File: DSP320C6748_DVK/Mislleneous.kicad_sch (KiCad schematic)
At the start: 45 parts, among them IC17 MUN5211DW1T1G, IC18 MUN5211DW1T1G, SW1 SW_DIP_x08

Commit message: Schematic Corrections-II Done
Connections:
- net +3V3D: now also R229.2, R230.2, R231.2, R232.2; no longer R261.1, R262.1
- net GND: no longer R229.2, R230.2, R231.2, R232.2
- new net +5V: R261.1, R262.1
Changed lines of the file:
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@@
 	)
 	(symbol
-		(lib_id "power:+3V3")
-		(at 257.81 121.92 90)
-		(unit 1)
-		(body_style 1)
-		(exclude_from_sim no)
-		(in_bom yes)
-		(on_board yes)
-		(in_pos_files yes)
-		(dnp no)
-		(fields_autoplaced yes)
-		(property "Reference" "#PWR0376"
-			(at 261.62 121.92 0)
-			(hide yes)
-			(show_name no)
-			(do_not_autoplace no)
-			(effects
-				(font
-					(size 1.27 1.27)
-				)
-			)
-		)
-		(property "Value" "+3V3D"
-			(at 252.73 121.92 0)
-			(show_name no)
-			(do_not_autoplace no)
-			(effects
-				(font
-					(size 1.27 1.27)
-				)
-			)
-		)
-		(property "Footprint" ""
-			(at 257.81 121.92 0)
-			(hide yes)
-			(show_name no)
-			(do_not_autoplace no)
-			(effects
-				(font
-					(size 1.27 1.27)
-				)
-			)
-		)
-		(property "Datasheet" ""
-			(at 257.81 121.92 0)
-			(hide yes)
-			(show_name no)
-			(do_not_autoplace no)
-			(effects
-				(font
-					(size 1.27 1.27)
-				)
-			)
-		)
-		(property "Description" "Power symbol creates a global label with name \"+3V3\""
-			(at 257.81 121.92 0)
-			(hide yes)
-			(show_name no)
-			(do_not_autoplace no)
-			(effects
-				(font
-					(size 1.27 1.27)
-				)
-			)
-		)
-		(pin "1"
-		)
-		(instances
-			(project "DSP320C6748_DVK"
-				(path "/3a70ffc0-9fe7-4a5b-b3c2-23140355df82/1866fe1a-a792-425d-9c22-4cbe8219f03e"
-					(reference "#PWR0376")
-					(unit 1)
-				)
-			)
-		)
-	)
-	(symbol
 		(lib_id "LOGSUN:LGS-KC-10-XX")
 		(at 195.58 146.05 270)
@@
 	)
 	(symbol
+		(lib_id "power:+5V")
+		(at 257.81 153.67 90)
+		(unit 1)
+		(body_style 1)
+		(exclude_from_sim no)
+		(in_bom yes)
+		(on_board yes)
+		(in_pos_files yes)
+		(dnp no)
+		(fields_autoplaced yes)
+		(property "Reference" "#PWR0389"
+			(at 261.62 153.67 0)
+			(hide yes)
+			(show_name no)
+			(do_not_autoplace no)
+			(effects
+				(font
+					(size 1.27 1.27)
+				)
+			)
+		)
+		(property "Value" "+5V"
+			(at 254 153.6699 90)
+			(show_name no)
+			(do_not_autoplace no)
+			(effects
+				(font
+					(size 1.27 1.27)
+				)
+				(justify left)
+			)
+		)
+		(property "Footprint" ""
+			(at 257.81 153.67 0)
+			(hide yes)
+			(show_name no)
+			(do_not_autoplace no)
+			(effects
+				(font
+					(size 1.27 1.27)
+				)
+			)
+		)
+		(property "Datasheet" ""
+			(at 257.81 153.67 0)
+			(hide yes)
+			(show_name no)
+			(do_not_autoplace no)
+			(effects
+				(font
+					(size 1.27 1.27)
+				)
+			)
+		)
+		(property "Description" "Power symbol creates a global label with name \"+5V\""
+			(at 257.81 153.67 0)
+			(hide yes)
+			(show_name no)
+			(do_not_autoplace no)
+			(effects
+				(font
+					(size 1.27 1.27)
+				)
+			)
+		)
+		(pin "1"
+		)
+		(instances
+			(project "DSP320C6748_DVK"
+				(path "/3a70ffc0-9fe7-4a5b-b3c2-23140355df82/1866fe1a-a792-425d-9c22-4cbe8219f03e"
+					(reference "#PWR0389")
+					(unit 1)
+				)
+			)
+		)
+	)
+	(symbol
 		(lib_id "Device:R_Small")
 		(at 243.84 119.38 0)
@@
 	)
 	(symbol
-		(lib_id "power:+3V3")
-		(at 257.81 153.67 90)
+		(lib_id "Device:R_Small")
+		(at 261.62 121.92 90)
 		(unit 1)
 		(body_style 1)
@@
 		(in_pos_files yes)
 		(dnp no)
-		(fields_autoplaced yes)
-		(property "Reference" "#PWR0377"
-			(at 261.62 153.67 0)
-			(hide yes)
+		(property "Reference" "R261"
+			(at 263.398 123.444 90)
 			(show_name no)
 			(do_not_autoplace no)
 			(effects
 				(font
-					(size 1.27 1.27)
+					(size 1.016 1.016)
 				)
+				(justify left)
 			)
 		)
-		(property "Value" "+3V3D"
-			(at 252.73 153.67 0)
+		(property "Value" "330R,5%,1/16W"
+			(at 268.732 118.11 90)
 			(show_name no)
 			(do_not_autoplace no)
@@
 					(size 1.27 1.27)
 				)
+				(justify left)
 			)
 		)
 		(property "Footprint" ""
-			(at 257.81 153.67 0)
+			(at 261.62 121.92 0)
 			(hide yes)
 			(show_name no)
@@
 		)
 		(property "Datasheet" ""
-			(at 257.81 153.67 0)
+			(at 261.62 121.92 0)
 			(hide yes)
 			(show_name no)
@@
 			)
 		)
-		(property "Description" "Power symbol creates a global label with name \"+3V3\""
-			(at 257.81 153.67 0)
+		(property "Description" "Resistor, small symbol"
+			(at 261.62 121.92 0)
 			(hide yes)
 			(show_name no)
@@
 			)
 		)
+		(pin "2"
+		)
 		(pin "1"
 		)
@@
 			(project "DSP320C6748_DVK"
 				(path "/3a70ffc0-9fe7-4a5b-b3c2-23140355df82/1866fe1a-a792-425d-9c22-4cbe8219f03e"
-					(reference "#PWR0377")
+					(reference "R261")
 					(unit 1)
 				)
@@
 	)
 	(symbol
-		(lib_id "power:GND")
-		(at 48.26 143.51 90)
+		(lib_id "power:+5V")
+		(at 257.81 121.92 90)
 		(unit 1)
 		(body_style 1)
@@
 		(in_pos_files yes)
 		(dnp no)
-		(property "Reference" "#PWR0364"
-			(at 54.61 143.51 0)
-			(hide yes)
-			(show_name no)
-			(do_not_autoplace no)
-			(effects
-				(font
-					(size 1.27 1.27)
-				)
-			)
-		)
-		(property "Value" "GND"
-			(at 51.816 143.51 0)
-			(show_name no)
-			(do_not_autoplace no)
-			(effects
-				(font
-					(size 1.27 1.27)
-				)
-			)
-		)
-		(property "Footprint" ""
-			(at 48.26 143.51 0)
+		(fields_autoplaced yes)
+		(property "Reference" "#PWR0356"
+			(at 261.62 121.92 0)
 			(hide yes)
 			(show_name no)
@@
 			)
 		)
-		(property "Datasheet" ""
-			(at 48.26 143.51 0)
-			(hide yes)
-			(show_name no)
-			(do_not_autoplace no)
-			(effects
-				(font
-					(size 1.27 1.27)
-				)
-			)
-		)
-		(property "Description" "Power symbol creates a global label with name \"GND\" , ground"
-			(at 48.26 143.51 0)
-			(hide yes)
-			(show_name no)
-			(do_not_autoplace no)
-			(effects
-				(font
-					(size 1.27 1.27)
-				)
-			)
-		)
-		(pin "1"
-		)
-		(instances
-			(project "DSP320C6748_DVK"
-				(path "/3a70ffc0-9fe7-4a5b-b3c2-23140355df82/1866fe1a-a792-425d-9c22-4cbe8219f03e"
-					(reference "#PWR0364")
-					(unit 1)
-				)
-			)
-		)
-	)
-	(symbol
-		(lib_id "Device:R_Small")
-		(at 261.62 121.92 90)
-		(unit 1)
-		(body_style 1)
-		(exclude_from_sim no)
-		(in_bom yes)
-		(on_board yes)
-		(in_pos_files yes)
-		(dnp no)
-		(property "Reference" "R261"
-			(at 263.398 123.444 90)
-			(show_name no)
-			(do_not_autoplace no)
-			(effects
-				(font
-					(size 1.016 1.016)
-				)
-				(justify left)
-			)
-		)
-		(property "Value" "330R,5%,1/16W"
-			(at 268.732 118.11 90)
+		(property "Value" "+5V"
+			(at 254 121.9199 90)
 			(show_name no)
 			(do_not_autoplace no)
@@
 		)
 		(property "Footprint" ""
-			(at 261.62 121.92 0)
+			(at 257.81 121.92 0)
 			(hide yes)
 			(show_name no)
@@
 		)
 		(property "Datasheet" ""
-			(at 261.62 121.92 0)
+			(at 257.81 121.92 0)
 			(hide yes)
 			(show_name no)
@@
 			)
 		)
-		(property "Description" "Resistor, small symbol"
-			(at 261.62 121.92 0)
+		(property "Description" "Power symbol creates a global label with name \"+5V\""
+			(at 257.81 121.92 0)
 			(hide yes)
 			(show_name no)
@@
 			)
 		)
-		(pin "2"
-		)
 		(pin "1"
 		)
@@
 			(project "DSP320C6748_DVK"
 				(path "/3a70ffc0-9fe7-4a5b-b3c2-23140355df82/1866fe1a-a792-425d-9c22-4cbe8219f03e"
-					(reference "R261")
+					(reference "#PWR0356")
 					(unit 1)
 				)
@@
 					(unit 1)
 				)
+			)
+		)
+	)
+	(symbol
+		(lib_id "power:+3V3")
+		(at 48.26 143.51 0)
+		(unit 1)
+		(body_style 1)
+		(exclude_from_sim no)
+		(in_bom yes)
+		(on_board yes)
+		(in_pos_files yes)
+		(dnp no)
+		(fields_autoplaced yes)
+		(property "Reference" "#PWR0384"
+			(at 48.26 147.32 0)
+			(hide yes)
+			(show_name no)
+			(do_not_autoplace no)
+			(effects
+				(font
+					(size 1.27 1.27)
+				)
+			)
+		)
+		(property "Value" "+3V3D"
+			(at 48.26 138.43 0)
+			(show_name no)
+			(do_not_autoplace no)
+			(effects
+				(font
+					(size 1.27 1.27)
+				)
+			)
+		)
+		(property "Footprint" ""
+			(at 48.26 143.51 0)
+			(hide yes)
+			(show_name no)
+			(do_not_autoplace no)
+			(effects
+				(font
+					(size 1.27 1.27)
+				)
+			)
+		)
+		(property "Datasheet" ""
+			(at 48.26 143.51 0)
+			(hide yes)
+			(show_name no)
+			(do_not_autoplace no)
+			(effects
+				(font
+					(size 1.27 1.27)
+				)
+			)
+		)
+		(property "Description" "Power symbol creates a global label with name \"+3V3\""
+			(at 48.26 143.51 0)
+			(hide yes)
+			(show_name no)
+			(do_not_autoplace no)
+			(effects
+				(font
+					(size 1.27 1.27)
+				)
+			)
+		)
+		(pin "1"
+		)
+		(instances
+			(project "DSP320C6748_DVK"
+				(path "/3a70ffc0-9fe7-4a5b-b3c2-23140355df82/1866fe1a-a792-425d-9c22-4cbe8219f03e"
+					(reference "#PWR0384")
+					(unit 1)
+				)

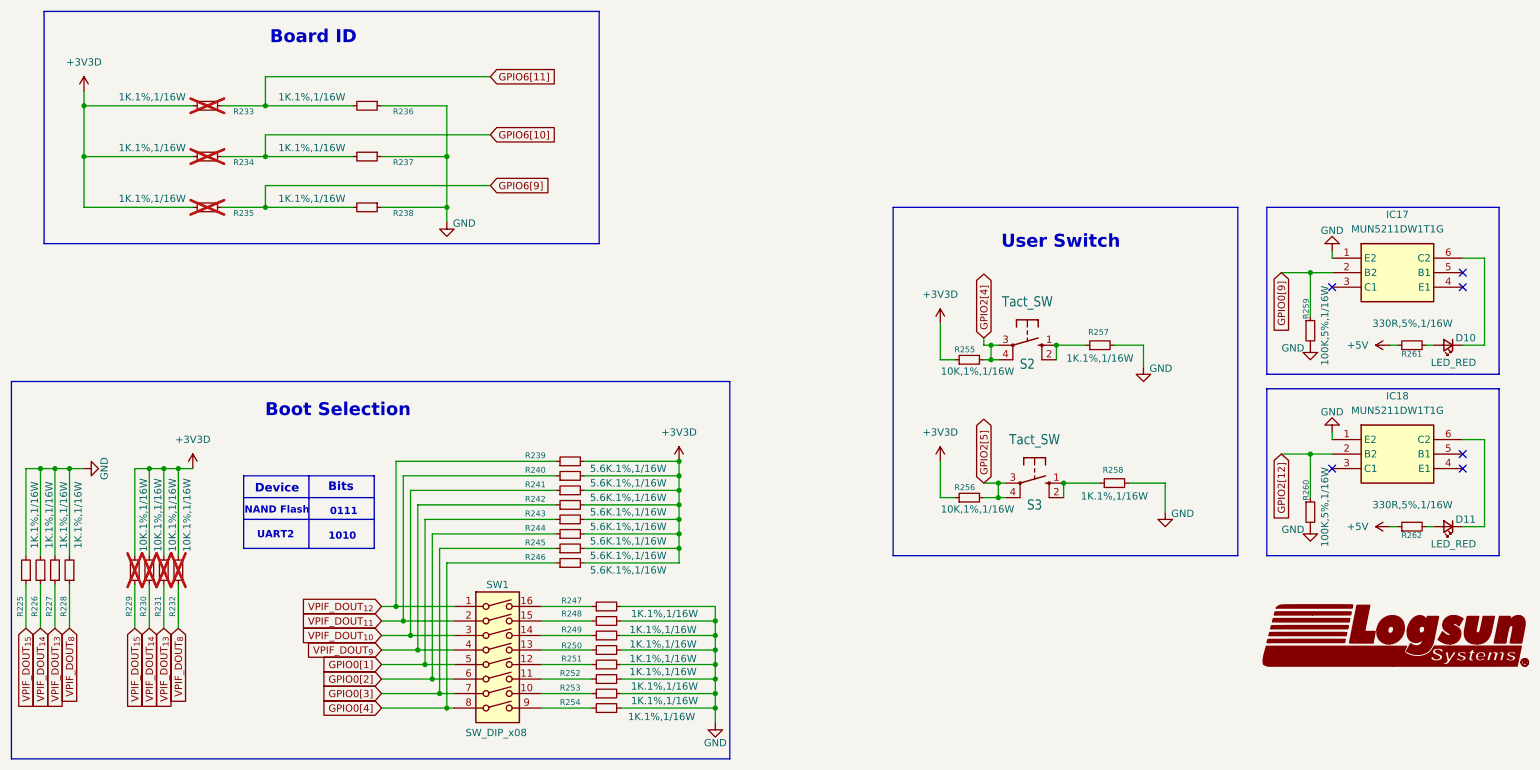
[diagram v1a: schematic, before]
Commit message: DC jack Replaced With Type-C, ADC and RTC section added
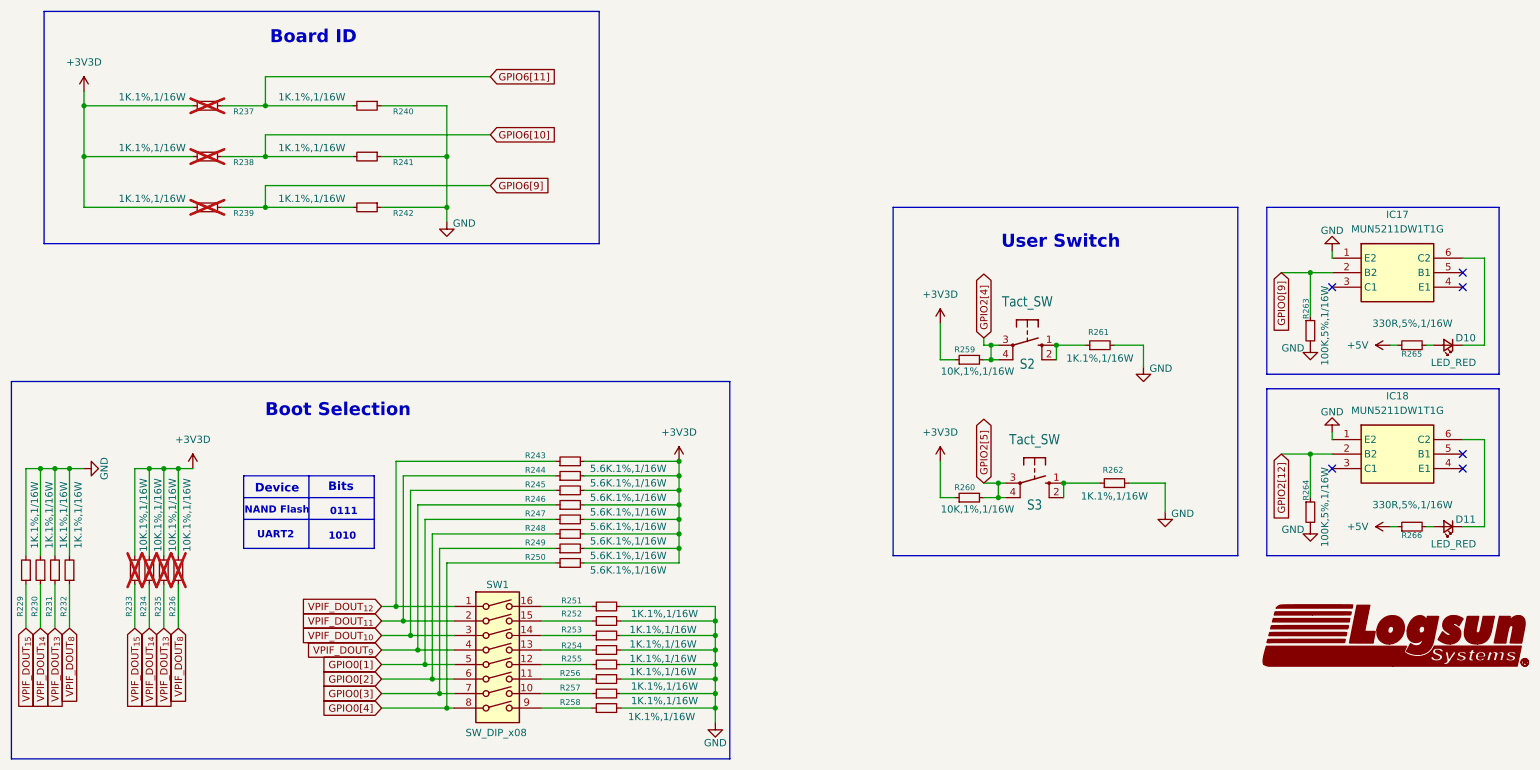
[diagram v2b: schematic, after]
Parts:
- renumbered R225 to R229, R226 to R230, R227 to R231, R228 to R232, R229 to R233, R230 to R234, R231 to R235, R232 to R236, R233 to R237, R234 to R238, R235 to R239, R236 to R240, R237 to R241, R238 to R242, R239 to R243, R240 to R244, R241 to R245, R242 to R246, R243 to R247, R244 to R248, R245 to R249, R246 to R250, R247 to R251, R248 to R252, R249 to R253, R250 to R254, R251 to R255, R252 to R256, R253 to R257, R254 to R258, R255 to R259, R256 to R260, R257 to R261, R258 to R262, R259 to R263, R260 to R264, R261 to R265, R262 to R266

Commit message: Scheamtic Re-annotation done, Some footprints assigned
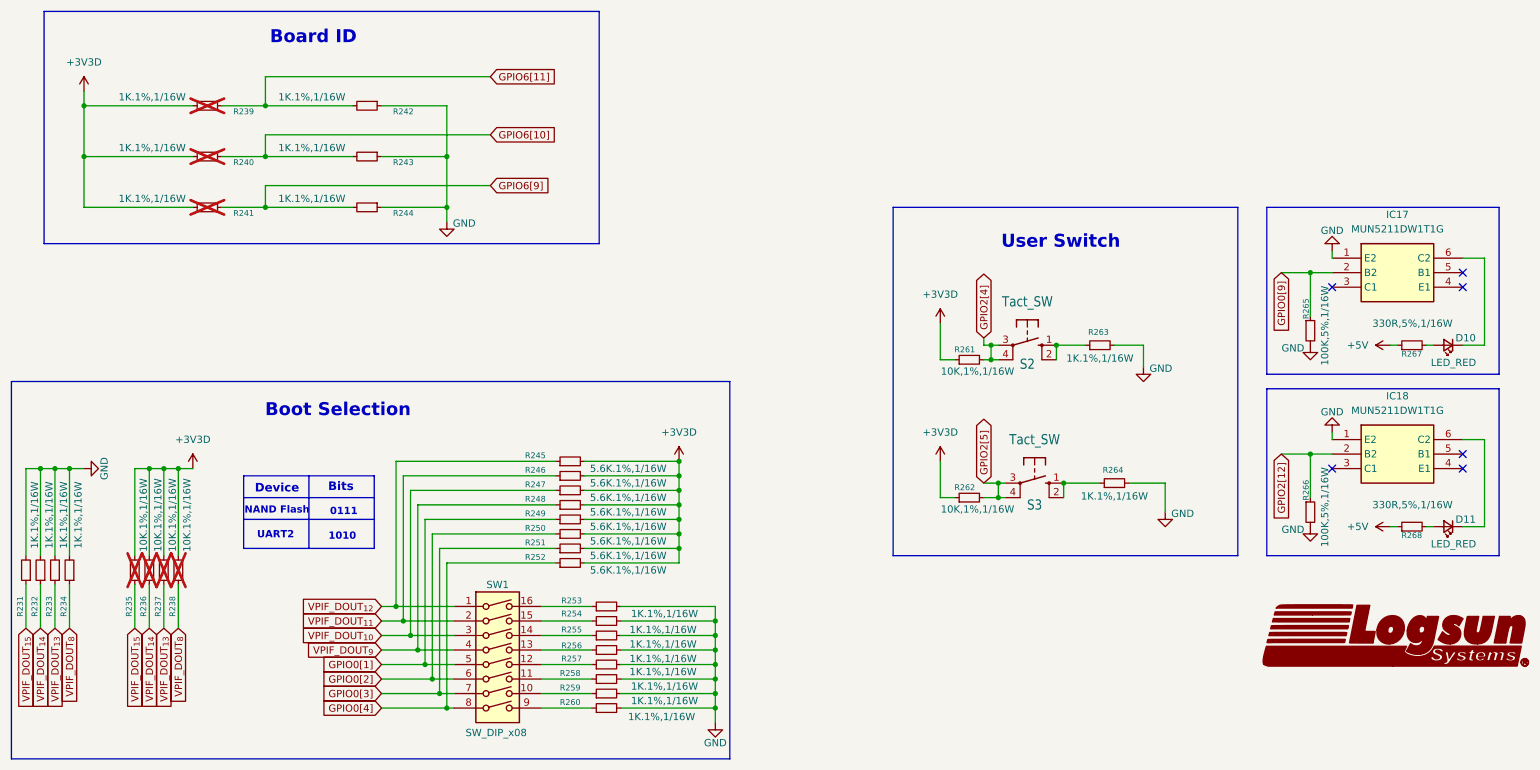
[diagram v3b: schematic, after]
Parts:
- R231: renamed from R229; footprint (none) -> Resistor_SMD:R_0603_1608Metric_Pad0.98x0.95mm_HandSolder
- R232: renamed from R230; footprint (none) -> Resistor_SMD:R_0603_1608Metric_Pad0.98x0.95mm_HandSolder
- R233: renamed from R231; footprint (none) -> Resistor_SMD:R_0603_1608Metric_Pad0.98x0.95mm_HandSolder
- R234: renamed from R232; footprint (none) -> Resistor_SMD:R_0603_1608Metric_Pad0.98x0.95mm_HandSolder
- R235: renamed from R233; footprint (none) -> Resistor_SMD:R_0603_1608Metric_Pad0.98x0.95mm_HandSolder
- R236: renamed from R234; footprint (none) -> Resistor_SMD:R_0603_1608Metric_Pad0.98x0.95mm_HandSolder
- R237: renamed from R235; footprint (none) -> Resistor_SMD:R_0603_1608Metric_Pad0.98x0.95mm_HandSolder
- R238: renamed from R236; footprint (none) -> Resistor_SMD:R_0603_1608Metric_Pad0.98x0.95mm_HandSolder
- R239: renamed from R237; footprint (none) -> Resistor_SMD:R_0603_1608Metric_Pad0.98x0.95mm_HandSolder
- R240: renamed from R238; footprint (none) -> Resistor_SMD:R_0603_1608Metric_Pad0.98x0.95mm_HandSolder
- R241: renamed from R239; footprint (none) -> Resistor_SMD:R_0603_1608Metric_Pad0.98x0.95mm_HandSolder
- R242: renamed from R240; footprint (none) -> Resistor_SMD:R_0603_1608Metric_Pad0.98x0.95mm_HandSolder
- R243: renamed from R241; footprint (none) -> Resistor_SMD:R_0603_1608Metric_Pad0.98x0.95mm_HandSolder
- R244: renamed from R242; footprint (none) -> Resistor_SMD:R_0603_1608Metric_Pad0.98x0.95mm_HandSolder
- R245: renamed from R243; footprint (none) -> Resistor_SMD:R_0603_1608Metric_Pad0.98x0.95mm_HandSolder
- R246: renamed from R244; footprint (none) -> Resistor_SMD:R_0603_1608Metric_Pad0.98x0.95mm_HandSolder
- R247: renamed from R245; footprint (none) -> Resistor_SMD:R_0603_1608Metric_Pad0.98x0.95mm_HandSolder
- R248: renamed from R246; footprint (none) -> Resistor_SMD:R_0603_1608Metric_Pad0.98x0.95mm_HandSolder
- R249: renamed from R247; footprint (none) -> Resistor_SMD:R_0603_1608Metric_Pad0.98x0.95mm_HandSolder
- R250: renamed from R248; footprint (none) -> Resistor_SMD:R_0603_1608Metric_Pad0.98x0.95mm_HandSolder
- R251: renamed from R249; footprint (none) -> Resistor_SMD:R_0603_1608Metric_Pad0.98x0.95mm_HandSolder
- R252: renamed from R250; footprint (none) -> Resistor_SMD:R_0603_1608Metric_Pad0.98x0.95mm_HandSolder
- R253: renamed from R251; footprint (none) -> Resistor_SMD:R_0603_1608Metric_Pad0.98x0.95mm_HandSolder
- R254: renamed from R252; footprint (none) -> Resistor_SMD:R_0603_1608Metric_Pad0.98x0.95mm_HandSolder
- R255: renamed from R253; footprint (none) -> Resistor_SMD:R_0603_1608Metric_Pad0.98x0.95mm_HandSolder
- R256: renamed from R254; footprint (none) -> Resistor_SMD:R_0603_1608Metric_Pad0.98x0.95mm_HandSolder
- R257: renamed from R255; footprint (none) -> Resistor_SMD:R_0603_1608Metric_Pad0.98x0.95mm_HandSolder
- R258: renamed from R256; footprint (none) -> Resistor_SMD:R_0603_1608Metric_Pad0.98x0.95mm_HandSolder
- R259: renamed from R257; footprint (none) -> Resistor_SMD:R_0603_1608Metric_Pad0.98x0.95mm_HandSolder
- R260: renamed from R258; footprint (none) -> Resistor_SMD:R_0603_1608Metric_Pad0.98x0.95mm_HandSolder
- R261: renamed from R259; footprint (none) -> Resistor_SMD:R_0603_1608Metric_Pad0.98x0.95mm_HandSolder
- R262: renamed from R260; footprint (none) -> Resistor_SMD:R_0603_1608Metric_Pad0.98x0.95mm_HandSolder
- R263: renamed from R261; footprint (none) -> Resistor_SMD:R_0603_1608Metric_Pad0.98x0.95mm_HandSolder
- R264: renamed from R262; footprint (none) -> Resistor_SMD:R_0603_1608Metric_Pad0.98x0.95mm_HandSolder
- R265: renamed from R263; footprint (none) -> Resistor_SMD:R_0603_1608Metric_Pad0.98x0.95mm_HandSolder
- R266: renamed from R264; footprint (none) -> Resistor_SMD:R_0603_1608Metric_Pad0.98x0.95mm_HandSolder
- R267: renamed from R265; footprint (none) -> Resistor_SMD:R_0603_1608Metric_Pad0.98x0.95mm_HandSolder
- R268: renamed from R266; footprint (none) -> Resistor_SMD:R_0603_1608Metric_Pad0.98x0.95mm_HandSolder
